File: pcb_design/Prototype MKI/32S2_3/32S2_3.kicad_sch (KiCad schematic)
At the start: 44 parts, among them J2 Micro_USB, Q1 Q_PNP_CBE, Q2 Q_PNP_CBE, SW1 NTC013-AT1J-A160T, SW2 NTC013-AT1J-A160T, U2 SGM2212-3.3XKC3G/TR

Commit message: Updated ESP32-S2 chip
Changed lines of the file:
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@@
   (symbol (lib_id "CPU:ESP32_S2_SOLO") (at 51.308 42.926 0) (unit 1)
     (in_bom yes) (on_board yes) (fields_autoplaced)
-    (property "Reference" "U?" (id 0) (at 84.836 24.1552 0))
-    (property "Value" "ESP32_S2_SOLO" (id 1) (at 84.836 26.6952 0))
+    (property "Reference" "U?" (id 0) (at 32.512 25.908 0))
+    (property "Value" "ESP32_S2_SOLO" (id 1) (at 52.07 25.908 0))
     (property "Footprint" "ESP-32-S2:ESP-32-S2-SOLO" (id 2) (at 24.13 17.526 0)
       (effects (font (size 1.27 1.27)) hide)
@@
     (pin "14")
     (pin "15")
+    (pin "27")
+    (pin "40")
+    (pin "28")
+    (pin "29")
+    (pin "30")
+    (pin "31")
+    (pin "32")
+    (pin "33")
+    (pin "34")
+    (pin "35")
+    (pin "36")
+    (pin "37")
+    (pin "38")
+    (pin "39")
     (pin "16")
     (pin "17")
@@
     (pin "25")
     (pin "26")
-    (pin "27")
-    (pin "28")
-    (pin "29")
     (pin "3")
-    (pin "30")
-    (pin "31")
-    (pin "32")
-    (pin "33")
-    (pin "34")
-    (pin "35")
-    (pin "36")
-    (pin "37")
-    (pin "38")
-    (pin "39")
     (pin "4")
-    (pin "40")
-    (pin "41")
-    (pin "42")
-    (pin "43")
-    (pin "44")
-    (pin "45")
-    (pin "46")
-    (pin "47")
-    (pin "48")
-    (pin "49")
     (pin "5")
-    (pin "50")
-    (pin "51")
-    (pin "52")
-    (pin "53")
-    (pin "54")
-    (pin "55")
-    (pin "56")
-    (pin "57")
     (pin "6")
     (pin "7")

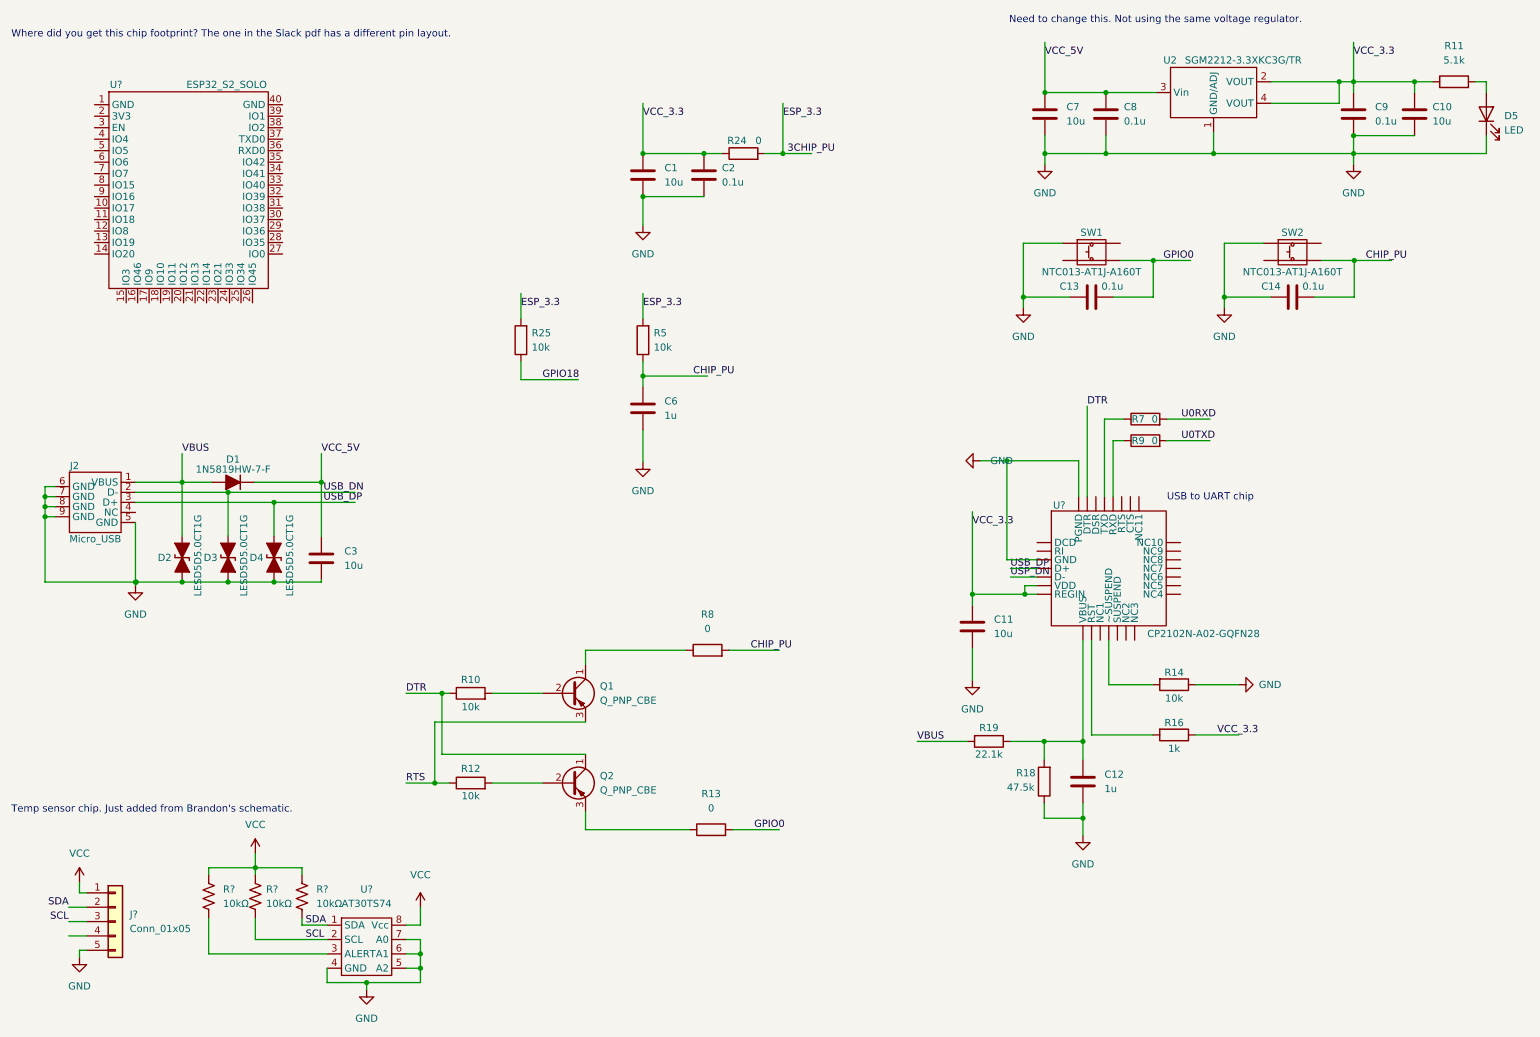
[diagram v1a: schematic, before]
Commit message: Added voltage regulator to schematic
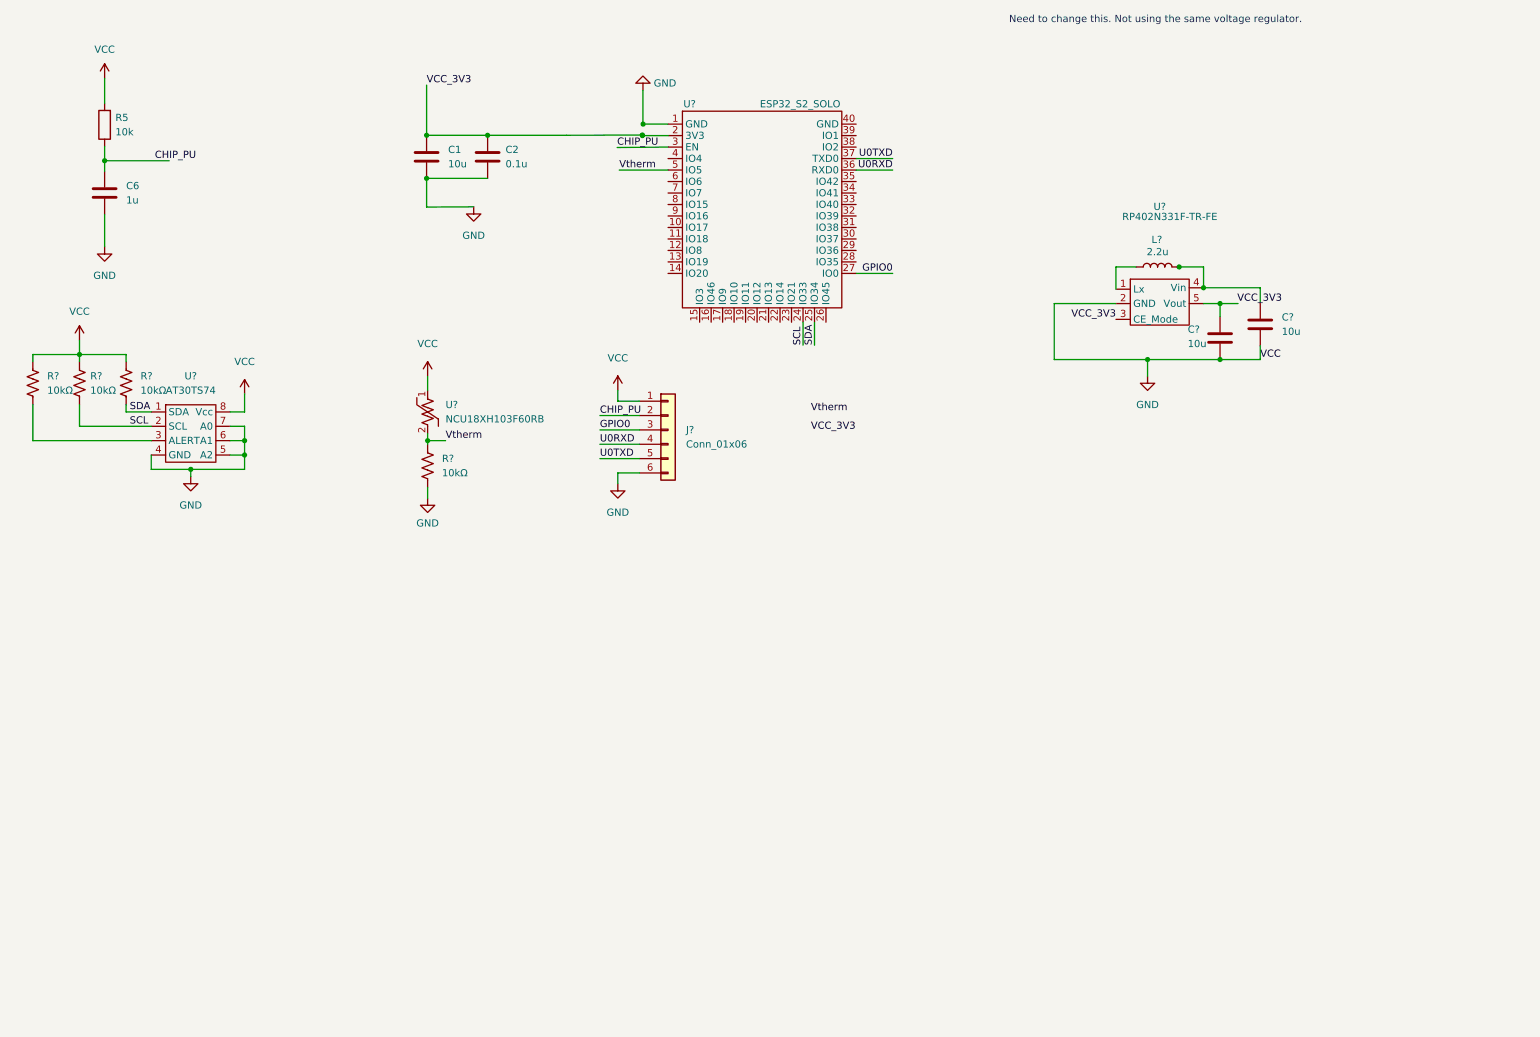
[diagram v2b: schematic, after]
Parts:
- removed C10, C11, C3, C7: 10u, symbol Device:C
- removed C12: 1u, symbol Device:C
- removed C13, C14, C8, C9: 0.1u, symbol Device:C
- removed D1: 1N5819HW-7-F, symbol Device:D_Filled
- removed D2, D3, D4: LESD5D5.0CT1G, symbol Device:D_TVS_Filled
- removed D5: LED, symbol Device:LED
- removed J2: Micro_USB, symbol Connector:Micro_USB
- removed J?: Conn_01x05, Connector_PinHeader_2.54mm:PinHeader_1x05_P2.54mm_Vertical, symbol Connector_Generic:Conn_01x05
- removed Q1, Q2: Q_PNP_CBE, symbol Device:Q_PNP_CBE
- removed R10, R12, R14, R25: 10k, symbol Device:R
- removed R11: 5.1k, symbol Device:R
- removed R13, R24, R7, R8, R9: 0, symbol Device:R
- removed R16: 1k, symbol Device:R
- removed R18: 47.5k, symbol Device:R
- removed R19: 22.1k, symbol Device:R
- removed SW1, SW2: NTC013-AT1J-A160T, symbol Switch:NTC013-AT1J-A160T
- removed U2: SGM2212-3.3XKC3G/TR, symbol Power_Protection:SGM2212-3.3XKC3G/TR
- removed U?: CP2102N-A02-GQFN28, symbol Device:CP2102N-A02-GQFN28
- added C? (x2): 10u, symbol Device:C
- added J?: Conn_01x06, symbol Connector_Generic:Conn_01x06
- added L?: 2.2u, symbol Device:L
- added R?: 10kΩ, Resistor_SMD:R_0805_2012Metric_Pad1.20x1.40mm_HandSolder, symbol Device:R_US
- added U?: NCU18XH103F60RB, Resistor_SMD:R_0805_2012Metric_Pad1.20x1.40mm_HandSolder, symbol Temp Sensors:NCU18XH103F60RB
- added U?: RP402N331F-TR-FE, Module:RP402N331F-TR-FE, symbol power:RP402N331F-TR-FE
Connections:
- net VCC is gone; now on net GND: R?.1, R?.1, R?.1, U?.8 (Vcc)
- net VCC_3.3 is gone; now on an unnamed net: C1.1, C2.1
- net GND: now also R5.2, U?.1 (GND), C?.1, C?.2, J?.1 (Pin_1), J?.6 (Pin_6), R?.2, U?.1, U?.2 (GND)
- net GPIO0: now also U?.27 (IO0), J?.3 (Pin_3)
- net SCL: now also U?.24 (IO33)
- net SDA: now also U?.25 (IO34)
- net U0RXD: now also U?.36 (RXD0), J?.4 (Pin_4)
- net U0TXD: now also U?.37 (TXD0), J?.5 (Pin_5)
- net CHIP_PU: now reaches U?.3 (EN)
- net CHIP_PU: now also C6.1, R5.1, J?.2 (Pin_2)
- net Vtherm: now reaches U?.5 (IO5)
- net Vtherm: now also R?.1, U?.2
- removed net 3: C6.1, R5.1, R5.2
- new net: L?.1, U?.1 (Lx)
- new net: C?.1, L?.2, U?.4 (Vin)
- new net VCC_3V3: C?.2, U?.3 (CE_Mode), U?.5 (Vout)
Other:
- note removed: "Temp sensor chip. Just added from Brandon's schematic."
- note removed: "USB to UART chip"
- note removed: "Where did you get this chip footprint? The one in the Slack pdf has a different pin layout."
- moved on the sheet: C1, C2, C6, R5, R?, U?

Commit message: finalized PCB
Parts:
- removed J?: Conn_01x06, symbol Connector_Generic:Conn_01x06
- added J?: Conn_01x08, symbol Connector_Generic:Conn_01x08
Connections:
- net CHIP_PU: now also J?.4 (Pin_4)
- net GND: now also J?.8 (Pin_8); no longer R5.2, R?.1, R?.1, R?.1, U?.1, U?.8 (Vcc)
- net GPIO0: now also J?.5 (Pin_5)
- net U0RXD: now also J?.6 (Pin_6)
- net U0TXD: now also J?.7 (Pin_7)
- net VCC_3V3: now also R?.1, R?.1, R?.1, U?.1, U?.8 (Vcc), J?.3 (Pin_3)
- net Vtherm: now also J?.2 (Pin_2)
- net VCC: now reaches C?.1, L?.2, U?.4 (Vin)
- net VCC: now also R5.2, J?.1 (Pin_1)

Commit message: Finalized schematic
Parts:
- C1, C2, C6: footprint (none) -> Capacitor_SMD:C_0805_2012Metric_Pad1.18x1.45mm_HandSolder
- C3, C4: renamed from C?; footprint (none) -> Capacitor_SMD:C_0805_2012Metric_Pad1.18x1.45mm_HandSolder
- J1: renamed from J?; footprint (none) -> Connector_PinHeader_1.00mm:PinHeader_1x08_P1.00mm_Vertical
- L1: renamed from L?; footprint (none) -> Inductor_SMD:L_0805_2012Metric_Pad1.05x1.20mm_HandSolder
- R5: footprint (none) -> Resistor_SMD:R_0805_2012Metric_Pad1.20x1.40mm_HandSolder
- U3: renamed from U?; footprint ESP-32-S2:ESP-32-S2-SOLO -> Module:ESP-32-S2-SOLO
- gave numbers to parts that had none: 7
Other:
- note removed: "Need to change this. Not using the same voltage regulator."

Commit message: v1 of PCB layout done
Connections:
- net U0RXD: now also J1.7 (Pin_7); no longer J1.6 (Pin_6)
- net U0TXD: now also J1.6 (Pin_6); no longer J1.7 (Pin_7)
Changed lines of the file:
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@@
     (effects (font (size 1.27 1.27)) (justify right bottom))
   )
-  (label "U0RXD" (at 144.78 97.155 180)
+  (label "U0RXD" (at 144.78 99.695 180)
     (effects (font (size 1.27 1.27)) (justify right bottom))
   )
@@
     (effects (font (size 1.27 1.27)) (justify right bottom))
   )
-  (label "U0TXD" (at 144.78 99.695 180)
-    (effects (font (size 1.27 1.27)) (justify right bottom))
-  )
   (label "SDA" (at 156.083 72.009 90)
     (effects (font (size 1.27 1.27)) (justify left bottom))
@@
     (effects (font (size 1.27 1.27)) (justify left bottom))
   )
+  (label "U0TXD" (at 144.78 97.155 180)
+    (effects (font (size 1.27 1.27)) (justify right bottom))
+  )
   (label "VCC" (at 239.903 61.849 0)
